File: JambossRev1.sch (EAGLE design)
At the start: 28 parts, among them CN1 1X4-BIG, CN2 1X4-BIG, J1 AVR_SPI_PRG_6NS, Q1 16MhZ, U1 MCP73831, U2 ATMEGA328P

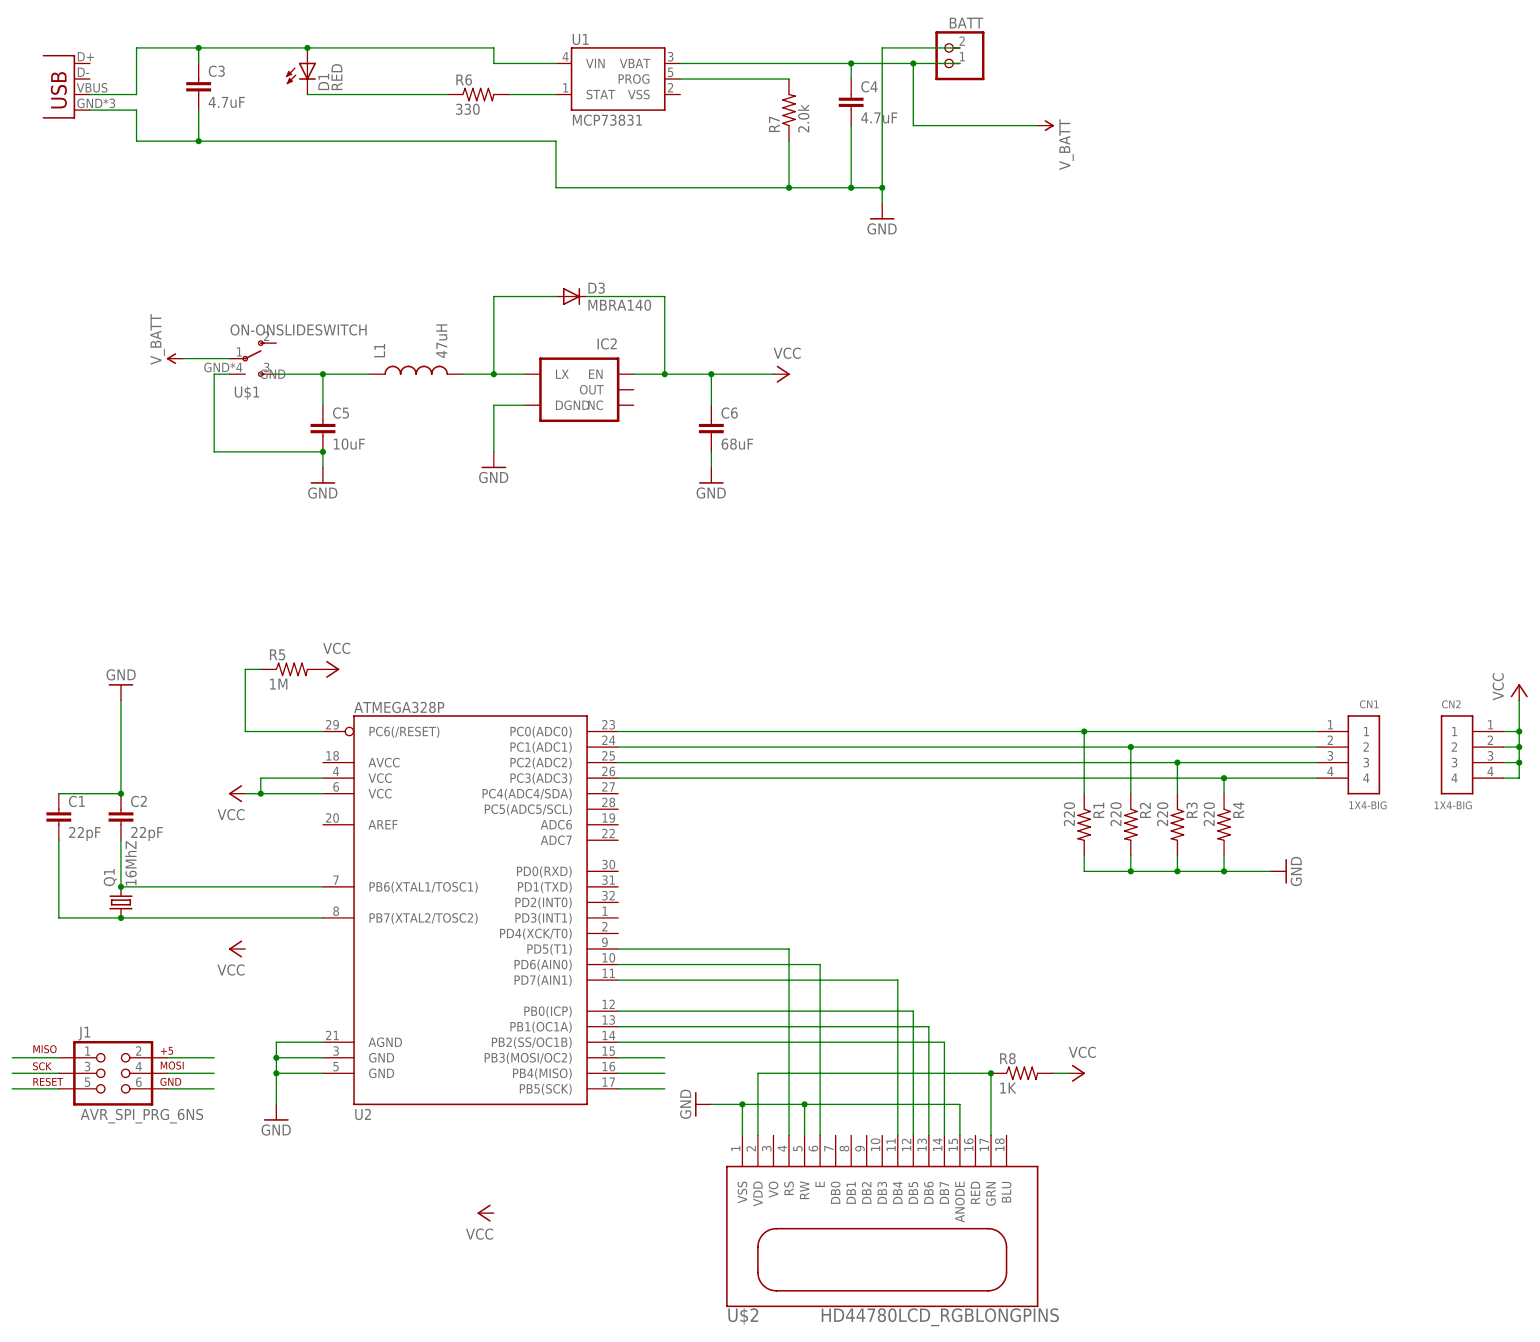
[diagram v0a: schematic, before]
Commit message: Board Layout
Improved silk readability
Moved the LCD resistor to the proper place
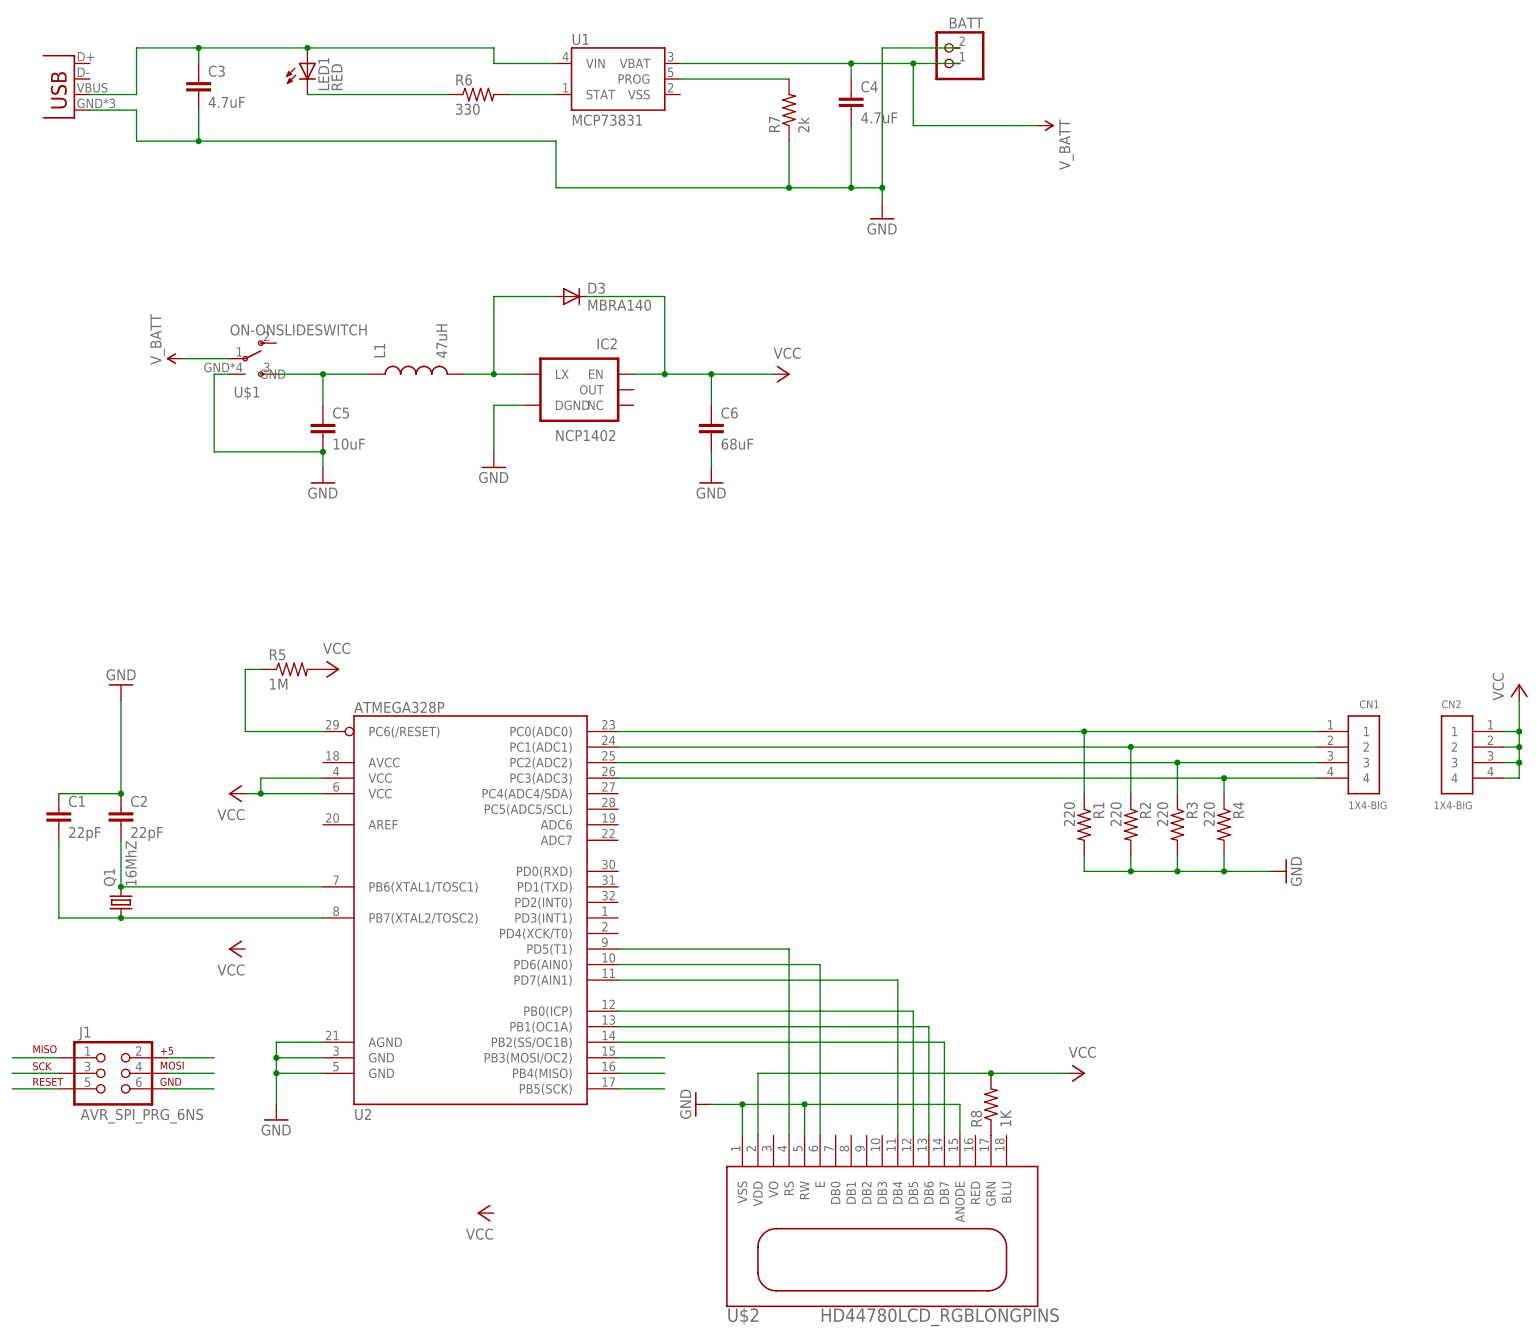
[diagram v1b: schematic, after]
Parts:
- IC2: value (none) -> NCP1402
- R7: value 2.0k -> 2k
- renumbered D1 to LED1
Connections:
- removed net VDD: R8.1, U$2.GRN, U$2.VDD
- new net GRN: R8.1, U$2.GRN
- net VCC: now also U$2.VDD
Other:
- moved on the sheet: R8
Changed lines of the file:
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@@
 <part name="R5" library="adafruit" deviceset="R-US_" device="R0603" value="1M"/>
 <part name="BATT" library="adafruit" deviceset="JST_2PIN" device="-THM-RA"/>
-<part name="D1" library="SparkFun-LED" deviceset="LED-RED" device="0603" value="RED"/>
+<part name="LED1" library="SparkFun-LED" deviceset="LED-RED" device="0603" value="RED"/>
 <part name="R6" library="SparkFun-Resistors" deviceset="330OHM1/10W1%(0603)" device="" value="330"/>
 <part name="C3" library="SparkFun-Capacitors" deviceset="4.7UF-6.3V-10%(0603)" device="0603" value="4.7uF"/>
-<part name="R7" library="SparkFun-Resistors" deviceset="2.0KOHM1/10W5%(0603)" device="" value="2.0k"/>
+<part name="R7" library="SparkFun-Resistors" deviceset="2.0KOHM1/10W5%(0603)" device="" value="2k"/>
 <part name="C4" library="SparkFun-Capacitors" deviceset="4.7UF-6.3V-10%(0603)" device="0603" value="4.7uF"/>
 <part name="SUPPLY3" library="SparkFun-Aesthetics" deviceset="V_BATT" device=""/>
@@
 <part name="C5" library="SparkFun-Capacitors" deviceset="10UF-6.3V-20%(1206)" device="" value="10uF"/>
 <part name="L1" library="SparkFun-Passives" deviceset="INDUCTOR" device="0805" value="47uH"/>
-<part name="IC2" library="SparkFun-PowerIC" deviceset="V_REG_NCP1400" device="SOT23-5"/>
+<part name="IC2" library="SparkFun-PowerIC" deviceset="V_REG_NCP1400" device="SOT23-5" value="NCP1402"/>
 <part name="D3" library="SparkFun-DiscreteSemi" deviceset="DIODE" device="SMA" value="MBRA140"/>
 <part name="C6" library="SparkFun-Passives" deviceset="CAP" device="0805" value="68uF"/>
@@
 <instance part="R5" gate="G$1" x="12.7" y="86.36"/>
 <instance part="BATT" gate="G$1" x="119.38" y="185.42" rot="MR0"/>
-<instance part="D1" gate="G$1" x="15.24" y="185.42"/>
+<instance part="LED1" gate="G$1" x="15.24" y="185.42"/>
 <instance part="R6" gate="G$1" x="43.18" y="180.34"/>
 <instance part="C3" gate="G$1" x="-2.54" y="180.34"/>
@@
 <instance part="U2" gate="G$1" x="40.64" y="50.8"/>
 <instance part="U$2" gate="G$1" x="109.22" y="-7.62"/>
-<instance part="R8" gate="G$1" x="132.08" y="20.32"/>
+<instance part="R8" gate="G$1" x="127" y="15.24" rot="R90"/>
 </instances>
 <busses>
@@
 <pinref part="VCC3" gate="VCC" pin="VCC"/>
 <pinref part="R8" gate="G$1" pin="2"/>
-<wire x1="137.16" y1="20.32" x2="139.7" y2="20.32" width="0.1524" layer="91"/>
+<wire x1="139.7" y1="20.32" x2="127" y2="20.32" width="0.1524" layer="91"/>
+<pinref part="U$2" gate="G$1" pin="VDD"/>
+<wire x1="88.9" y1="10.16" x2="88.9" y2="20.32" width="0.1524" layer="91"/>
+<wire x1="127" y1="20.32" x2="88.9" y2="20.32" width="0.1524" layer="91"/>
+<junction x="127" y="20.32"/>
 </segment>
 </net>
@@
 <net name="N$8" class="0">
 <segment>
-<pinref part="D1" gate="G$1" pin="C"/>
+<pinref part="LED1" gate="G$1" pin="C"/>
 <wire x1="15.24" y1="180.34" x2="38.1" y2="180.34" width="0.1524" layer="91"/>
 <pinref part="R6" gate="G$1" pin="1"/>
@@
 <pinref part="C3" gate="G$1" pin="1"/>
 <wire x1="-2.54" y1="187.96" x2="-2.54" y2="185.42" width="0.1524" layer="91"/>
-<pinref part="D1" gate="G$1" pin="A"/>
+<pinref part="LED1" gate="G$1" pin="A"/>
 <wire x1="15.24" y1="187.96" x2="45.72" y2="187.96" width="0.1524" layer="91"/>
 <wire x1="45.72" y1="187.96" x2="45.72" y2="185.42" width="0.1524" layer="91"/>
@@
 </segment>
 </net>
-<net name="VDD" class="1">
+<net name="GRN" class="1">
 <segment>
 <pinref part="U$2" gate="G$1" pin="GRN"/>
 <pinref part="R8" gate="G$1" pin="1"/>
-<wire x1="127" y1="20.32" x2="127" y2="10.16" width="0.1524" layer="91"/>
-<pinref part="U$2" gate="G$1" pin="VDD"/>
-<wire x1="88.9" y1="10.16" x2="88.9" y2="20.32" width="0.1524" layer="91"/>
-<wire x1="88.9" y1="20.32" x2="127" y2="20.32" width="0.1524" layer="91"/>
-<junction x="127" y="20.32"/>
-</segment>
-</net>
+</segment>
+</net>

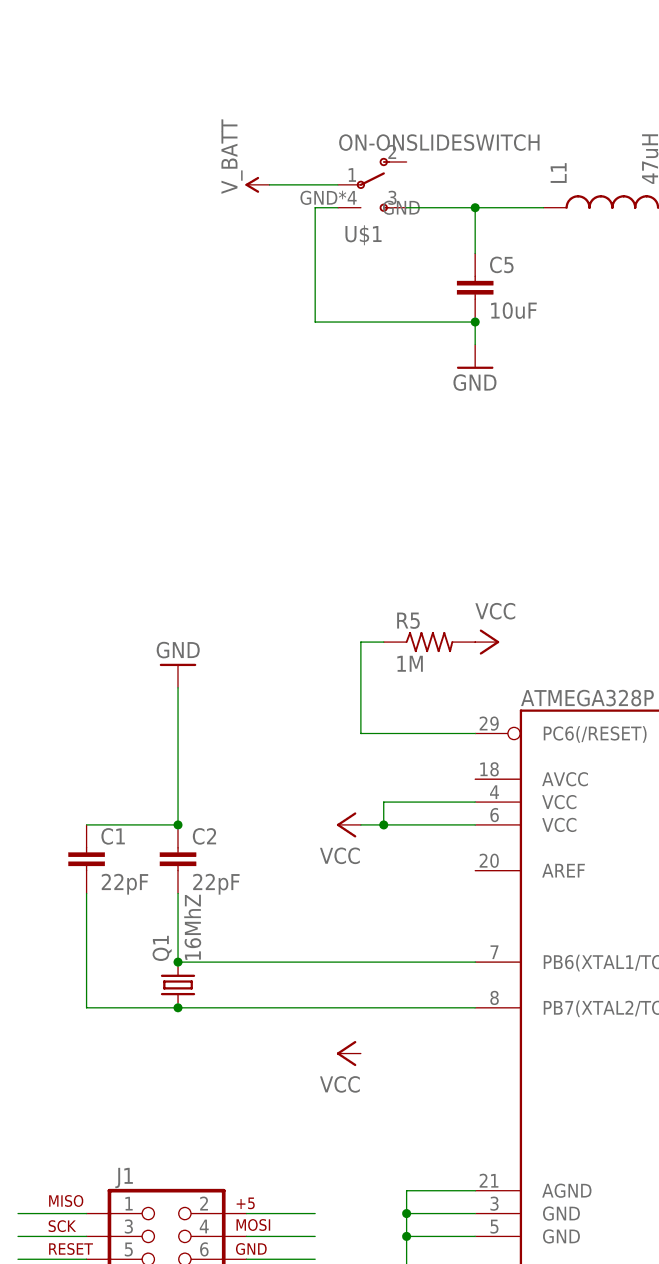
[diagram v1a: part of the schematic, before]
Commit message: Switch, silkscreen, xtal
Fixed on/off switch connections
Swapped xtal for identical with smaller footprint, shorter profile
(saved 3 cents)
Arranged silk labels for easier reading
Added OSH logo and github URL to bottom silk
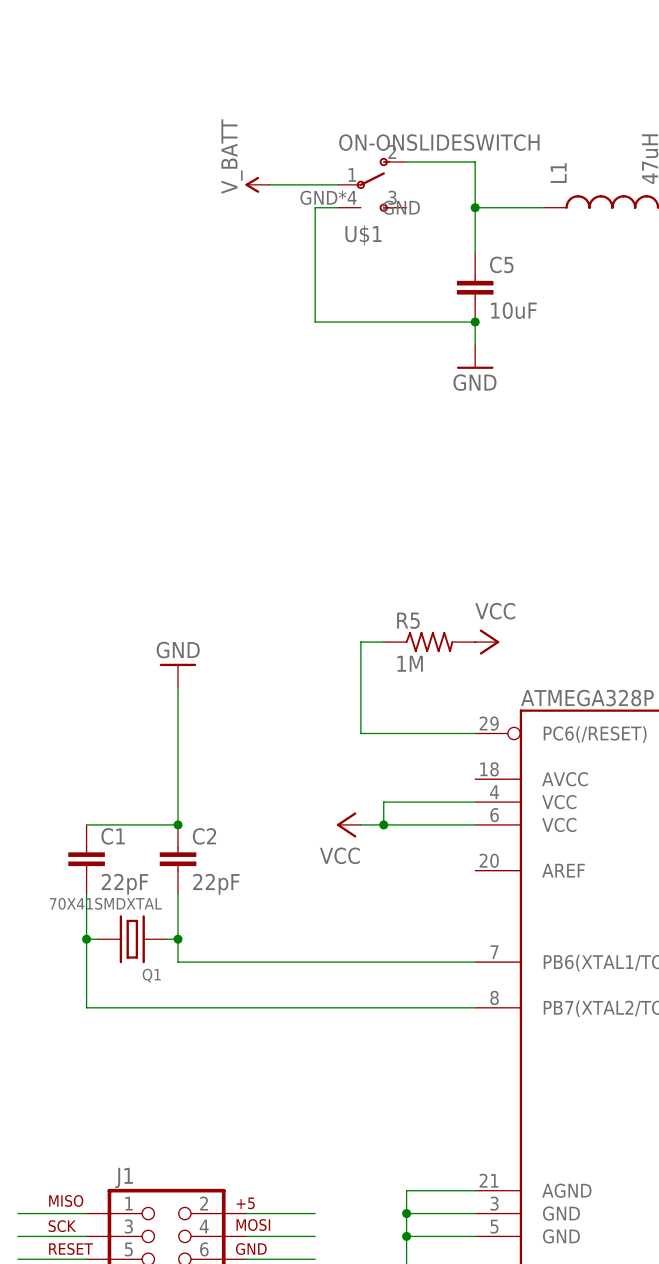
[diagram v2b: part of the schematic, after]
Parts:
- Q1: value 16MhZ -> 70X41SMDXTAL; device SparkFun-FreqCtrl:CRYSTALSMD -> iconcustom:70X41SMDXTAL
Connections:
- net N$1: now also Q1.P$1; no longer Q1.2
- net N$2: now also Q1.P$2; no longer Q1.1
- net N$22: now also U$1.2; no longer U$1.3
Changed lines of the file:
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@@
 </classes>
 <parts>
-<part name="VCC" library="supply1" deviceset="VCC" device=""/>
 <part name="VCC2" library="supply1" deviceset="VCC" device=""/>
 <part name="GND1" library="supply1" deviceset="GND" device=""/>
 <part name="GND2" library="supply1" deviceset="GND" device=""/>
-<part name="Q1" library="SparkFun-FreqCtrl" deviceset="CRYSTAL" device="SMD" value="16MhZ"/>
 <part name="C1" library="SparkFun-Capacitors" deviceset="CAP" device="0805" value="22pF"/>
 <part name="C2" library="SparkFun-Capacitors" deviceset="CAP" device="0805" value="22pF"/>
@@
 <part name="U$2" library="adafruit" deviceset="HD44780LCD_RGB" device="LONGPINS"/>
 <part name="R8" library="SparkFun-Resistors" deviceset="RESISTOR" device="0805-RES" value="1K"/>
+<part name="Q1" library="iconcustom" deviceset="70X41SMDXTAL" device=""/>
 </parts>
 <sheets>
@@
 </plain>
 <instances>
-<instance part="VCC" gate="VCC" x="2.54" y="40.64" rot="R90"/>
 <instance part="VCC2" gate="VCC" x="2.54" y="66.04" rot="R90"/>
 <instance part="GND1" gate="1" x="10.16" y="12.7"/>
 <instance part="GND2" gate="1" x="-15.24" y="83.82" rot="R180"/>
-<instance part="Q1" gate="G$1" x="-15.24" y="48.26" rot="R90"/>
 <instance part="C1" gate="G$1" x="-25.4" y="60.96"/>
 <instance part="C2" gate="G$1" x="-15.24" y="60.96"/>
@@
 <instance part="U$2" gate="G$1" x="109.22" y="-7.62"/>
 <instance part="R8" gate="G$1" x="127" y="15.24" rot="R90"/>
+<instance part="Q1" gate="Q1" x="-20.32" y="53.34" rot="R180"/>
 </instances>
 <busses>
@@
 <net name="N$1" class="0">
 <segment>
-<pinref part="Q1" gate="G$1" pin="2"/>
 <wire x1="17.78" y1="50.8" x2="-15.24" y2="50.8" width="0.1524" layer="91"/>
-<wire x1="-15.24" y1="50.8" x2="-15.24" y2="58.42" width="0.1524" layer="91"/>
-<junction x="-15.24" y="50.8"/>
+<pinref part="U2" gate="G$1" pin="PB6(XTAL1/TOSC1)"/>
 <pinref part="C2" gate="G$1" pin="2"/>
-<pinref part="U2" gate="G$1" pin="PB6(XTAL1/TOSC1)"/>
+<wire x1="-15.24" y1="58.42" x2="-15.24" y2="53.34" width="0.1524" layer="91"/>
+<pinref part="Q1" gate="Q1" pin="P$1"/>
+<wire x1="-15.24" y1="53.34" x2="-15.24" y2="50.8" width="0.1524" layer="91"/>
+<wire x1="-15.24" y1="53.34" x2="-16.51" y2="53.34" width="0.1524" layer="91"/>
+<junction x="-15.24" y="53.34"/>
 </segment>
 </net>
 <net name="N$2" class="0">
 <segment>
-<pinref part="Q1" gate="G$1" pin="1"/>
-<wire x1="17.78" y1="45.72" x2="-15.24" y2="45.72" width="0.1524" layer="91"/>
+<wire x1="17.78" y1="45.72" x2="-25.4" y2="45.72" width="0.1524" layer="91"/>
+<pinref part="U2" gate="G$1" pin="PB7(XTAL2/TOSC2)"/>
 <pinref part="C1" gate="G$1" pin="2"/>
-<wire x1="-15.24" y1="45.72" x2="-25.4" y2="45.72" width="0.1524" layer="91"/>
-<wire x1="-25.4" y1="45.72" x2="-25.4" y2="58.42" width="0.1524" layer="91"/>
-<junction x="-15.24" y="45.72"/>
-<pinref part="U2" gate="G$1" pin="PB7(XTAL2/TOSC2)"/>
+<wire x1="-25.4" y1="58.42" x2="-25.4" y2="53.34" width="0.1524" layer="91"/>
+<pinref part="Q1" gate="Q1" pin="P$2"/>
+<wire x1="-25.4" y1="53.34" x2="-25.4" y2="45.72" width="0.1524" layer="91"/>
+<wire x1="-25.4" y1="53.34" x2="-24.13" y2="53.34" width="0.1524" layer="91"/>
+<junction x="-25.4" y="53.34"/>
 </segment>
 </net>
@@
 <pinref part="L1" gate="G$1" pin="1"/>
 <wire x1="17.78" y1="134.62" x2="25.4" y2="134.62" width="0.1524" layer="91"/>
-<pinref part="U$1" gate="G$1" pin="3"/>
-<wire x1="10.16" y1="134.62" x2="17.78" y2="134.62" width="0.1524" layer="91"/>
 <junction x="17.78" y="134.62"/>
-</segment>
-</net>
+<pinref part="U$1" gate="G$1" pin="2"/>
+<wire x1="10.16" y1="139.7" x2="17.78" y2="139.7" width="0.1524" layer="91"/>
+<wire x1="17.78" y1="139.7" x2="17.78" y2="134.62" width="0.1524" layer="91"/>
+</segment>
+</net>
